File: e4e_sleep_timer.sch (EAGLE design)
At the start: 0 parts

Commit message: Added regulator, external power
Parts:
- added P1: XT60, XT60:XT60
- added U1: NUCLEO-G071RB, NUCLEO-F401RE:NUCLEO-G071RB
- added U2: 1224-5-150W, KNACRO_Regulator:1224-5-150W
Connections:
- new net +5V: U1G$1.E5V, U2.VOUT
- new net GND: P1.GND, U1G$1.GND_S1, U1G$2.AGND, U1G$2.GND_S2, U2.GND
- new net VEXT: P1.VCC, U2.VIN
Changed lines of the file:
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@@
 <parts>
 <part name="FRAME1" library="frames" library_urn="urn:adsk.eagle:library:229" deviceset="LETTER_L" device=""/>
+<part name="U1" library="NUCLEO-F401RE" deviceset="NUCLEO-G071RB" device=""/>
+<part name="SUPPLY1" library="supply2" library_urn="urn:adsk.eagle:library:372" deviceset="GND" device=""/>
+<part name="SUPPLY2" library="supply2" library_urn="urn:adsk.eagle:library:372" deviceset="GND" device=""/>
+<part name="P+1" library="supply1" library_urn="urn:adsk.eagle:library:371" deviceset="+5V" device=""/>
+<part name="FRAME2" library="frames" library_urn="urn:adsk.eagle:library:229" deviceset="LETTER_L" device=""/>
+<part name="P1" library="XT60" deviceset="XT60" device=""/>
+<part name="SUPPLY4" library="supply2" library_urn="urn:adsk.eagle:library:372" deviceset="GND" device=""/>
+<part name="U2" library="KNACRO_Regulator" deviceset="1224-5-150W" device=""/>
+<part name="SUPPLY5" library="supply2" library_urn="urn:adsk.eagle:library:372" deviceset="GND" device=""/>
+<part name="P+2" library="supply1" library_urn="urn:adsk.eagle:library:371" deviceset="+5V" device=""/>
 </parts>
 <sheets>
+<sheet>
+<plain>
+</plain>
+<instances>
+<instance part="FRAME2" gate="G$1" x="0" y="0" smashed="yes"/>
+<instance part="FRAME2" gate="G$2" x="147.32" y="0" smashed="yes">
+<attribute name="LAST_DATE_TIME" x="160.02" y="1.27" size="2.54" layer="94"/>
+<attribute name="SHEET" x="233.68" y="1.27" size="2.54" layer="94"/>
+<attribute name="DRAWING_NAME" x="165.1" y="19.05" size="2.54" layer="94"/>
+</instance>
+<instance part="P1" gate="G$1" x="25.4" y="160.02" smashed="yes" rot="R180"/>
+<instance part="SUPPLY4" gate="GND" x="30.48" y="154.94" smashed="yes">
+<attribute name="VALUE" x="28.575" y="151.765" size="1.778" layer="96"/>
+</instance>
+<instance part="U2" gate="G$1" x="106.68" y="160.02" smashed="yes">
+<attribute name="NAME" x="96.52" y="165.1" size="1.778" layer="95"/>
+<attribute name="VALUE" x="96.52" y="147.32" size="1.778" layer="96"/>
+</instance>
+<instance part="SUPPLY5" gate="GND" x="91.44" y="152.4" smashed="yes">
+<attribute name="VALUE" x="89.535" y="149.225" size="1.778" layer="96"/>
+</instance>
+<instance part="P+2" gate="1" x="129.54" y="167.64" smashed="yes">
+<attribute name="VALUE" x="127" y="162.56" size="1.778" layer="96" rot="R90"/>
+</instance>
+</instances>
+<busses>
+</busses>
+<nets>
+<net name="VEXT" class="0">
+<segment>
+<pinref part="P1" gate="G$1" pin="VCC"/>
+<wire x1="30.48" y1="162.56" x2="38.1" y2="162.56" width="0.1524" layer="91"/>
+<label x="38.1" y="162.56" size="1.778" layer="95"/>
+</segment>
+<segment>
+<pinref part="U2" gate="G$1" pin="VIN"/>
+<wire x1="91.44" y1="160.02" x2="81.28" y2="160.02" width="0.1524" layer="91"/>
+<label x="81.28" y="160.02" size="1.778" layer="95"/>
+</segment>
+</net>
+<net name="GND" class="0">
+<segment>
+<pinref part="P1" gate="G$1" pin="GND"/>
+<pinref part="SUPPLY4" gate="GND" pin="GND"/>
+</segment>
+<segment>
+<pinref part="U2" gate="G$1" pin="GND"/>
+<pinref part="SUPPLY5" gate="GND" pin="GND"/>
+</segment>
+</net>
+<net name="+5V" class="0">
+<segment>
+<pinref part="U2" gate="G$1" pin="VOUT"/>
+<wire x1="121.92" y1="160.02" x2="129.54" y2="160.02" width="0.1524" layer="91"/>
+<pinref part="P+2" gate="1" pin="+5V"/>
+<wire x1="129.54" y1="165.1" x2="129.54" y2="160.02" width="0.1524" layer="91"/>
+</segment>
+</net>
+</nets>
+</sheet>
 <sheet>
 <plain>
@@
 <attribute name="DRAWING_NAME" x="165.1" y="19.05" size="2.54" layer="94"/>
 </instance>
+<instance part="U1" gate="G$4" x="17.78" y="152.4" smashed="yes">
+<attribute name="NAME" x="12.7" y="166.37" size="1.778" layer="95"/>
+<attribute name="VALUE" x="12.7" y="138.43" size="1.778" layer="96" rot="MR180"/>
+</instance>
+<instance part="U1" gate="G$5" x="48.26" y="152.4" smashed="yes">
+<attribute name="NAME" x="43.18" y="161.29" size="1.778" layer="95"/>
+<attribute name="VALUE" x="43.18" y="140.97" size="1.778" layer="96" rot="MR180"/>
+</instance>
+<instance part="U1" gate="G$1" x="55.88" y="78.74" smashed="yes">
+<attribute name="NAME" x="40.64" y="120.65" size="1.778" layer="95"/>
+<attribute name="VALUE" x="40.64" y="34.29" size="1.778" layer="96" rot="MR180"/>
+</instance>
+<instance part="U1" gate="G$2" x="124.46" y="81.28" smashed="yes">
+<attribute name="NAME" x="111.76" y="120.65" size="1.778" layer="95"/>
+<attribute name="VALUE" x="111.76" y="39.37" size="1.778" layer="96" rot="MR180"/>
+</instance>
+<instance part="U1" gate="G$3" x="175.26" y="132.08" smashed="yes">
+<attribute name="NAME" x="165.1" y="148.59" size="1.778" layer="95"/>
+<attribute name="VALUE" x="165.1" y="113.03" size="1.778" layer="96" rot="MR180"/>
+</instance>
+<instance part="U1" gate="G$6" x="220.98" y="129.54" smashed="yes">
+<attribute name="NAME" x="210.82" y="140.97" size="1.778" layer="95"/>
+<attribute name="VALUE" x="210.82" y="115.57" size="1.778" layer="96" rot="MR180"/>
+</instance>
+<instance part="SUPPLY1" gate="GND" x="76.2" y="35.56" smashed="yes">
+<attribute name="VALUE" x="74.295" y="32.385" size="1.778" layer="96"/>
+</instance>
+<instance part="SUPPLY2" gate="GND" x="142.24" y="40.64" smashed="yes">
+<attribute name="VALUE" x="140.335" y="37.465" size="1.778" layer="96"/>
+</instance>
+<instance part="P+1" gate="1" x="81.28" y="116.84" smashed="yes">
+<attribute name="VALUE" x="78.74" y="111.76" size="1.778" layer="96" rot="R90"/>
+</instance>
 </instances>
 <busses>
 </busses>
 <nets>
+<net name="GND" class="0">
+<segment>
+<pinref part="U1" gate="G$1" pin="GND_S1"/>
+<pinref part="SUPPLY1" gate="GND" pin="GND"/>
+</segment>
+<segment>
+<pinref part="U1" gate="G$2" pin="GND_S2"/>
+<pinref part="SUPPLY2" gate="GND" pin="GND"/>
+<pinref part="U1" gate="G$2" pin="AGND"/>
+<wire x1="142.24" y1="45.72" x2="142.24" y2="43.18" width="0.1524" layer="91"/>
+<junction x="142.24" y="43.18"/>
+</segment>
+</net>
+<net name="+5V" class="0">
+<segment>
+<pinref part="P+1" gate="1" pin="+5V"/>
+<wire x1="81.28" y1="114.3" x2="81.28" y2="111.76" width="0.1524" layer="91"/>
+<pinref part="U1" gate="G$1" pin="E5V"/>
+<wire x1="81.28" y1="111.76" x2="76.2" y2="111.76" width="0.1524" layer="91"/>
+</segment>
+</net>
 </nets>
 </sheet>

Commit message: Completed PCB design
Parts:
- added P2: 10129378-906001BLF, con-lstb:MA06-1
- added P3: XT30PW-F, XT60:XT30PW-F
- added Q1: PJA3416AE_R1_00001, PJA3416AE_R1_00001:PJA3416AE_R1_00001
- added R1, R2, R5: 0, rcl:R-EU_R0603
- added R3: 100, rcl:R-US_R0603
- added R4: 10k, rcl:R-US_R0603
- added TP1, TP10, TP2, TP3, TP4, TP5, TP6, TP7, TP8, TP9: TPPAD1-13, testpad:TPPAD1-13
- added U$5: FH-320-NV, fuses:FH-320-NV
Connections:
- new net N$1: P2.4, R1.2, TP4.TP
- new net N$2: Q1.G, R3.1
- new net N$3: P2.5, R2.2
- new net N$4: R3.2, R4.1, R5.2
- new net N$5: Q1.D, U$5.G
- new net SYS_PWR: R5.1, TP6.TP, U1G$2.PD9
- new net USART1_RXD: R1.1, U1G$2.PC5
- new net USART1_TXD: R2.1, TP5.TP, U1G$2.PC4
- new net VDD1: P3.VCC, Q1.S, TP3.TP
- net +5V: now also TP2.TP, U$5.H
- net GND: now also P2.1, P3.GND, R4.2, TP10.TP, TP7.TP, TP8.TP, TP9.TP
- net VEXT: now also TP1.TP
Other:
- note added: "Control Port"
- note added: "MCU"
- moved on the sheet: U1G$1, U1G$2, U1G$3, U1G$4, U1G$5, U1G$6

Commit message: Finished PCB review
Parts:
- removed U$5: FH-320-NV, fuses:FH-320-NV
- added Q2: PJA3416AE_R1_00001, PJA3416AE_R1_00001:PJA3416AE_R1_00001
- added R6: 0, rcl:R-EU_R0603
- added TP11, TP12, TP13, TP14: TPTP20R, testpad:TPTP20R
- added U5: FH-320-NV, fuses:FH-320-NV
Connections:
- new net N$6: TP11.TP, U1G$1.VIN_S1
- new net N$7: R6.1, U1G$2.AGND
- new net N$8: TP13.TP, U1G$2.U5V
- new net N$9: TP14.TP, U1G$1.VBAT
- net +5V: now also U5.H; no longer U$5.H
- net GND: now also R6.2; no longer U1G$2.AGND
- net N$2: now also Q2.G
- net N$5: now also Q2.D, TP12.TP, U5.G; no longer U$5.G
- net VDD1: now also Q2.S
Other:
- moved on the sheet: P2, Q1, R1, R2, R3, R4, R5, TP4, TP5, TP6

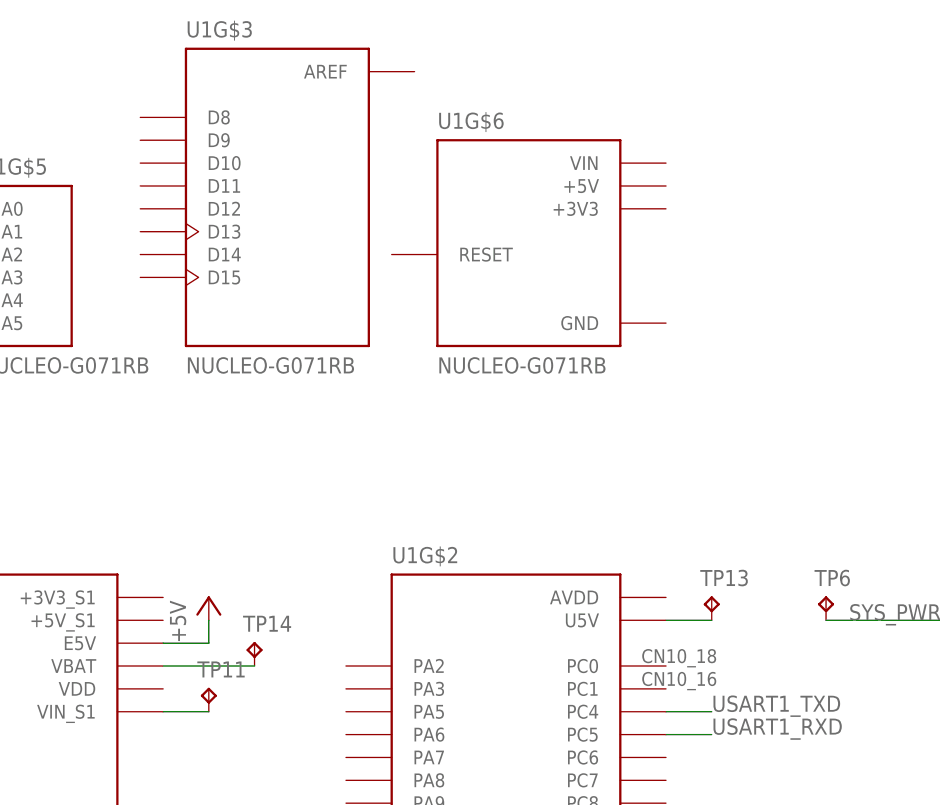
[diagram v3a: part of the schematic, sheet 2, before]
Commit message: Added Nucleo Board power bypass
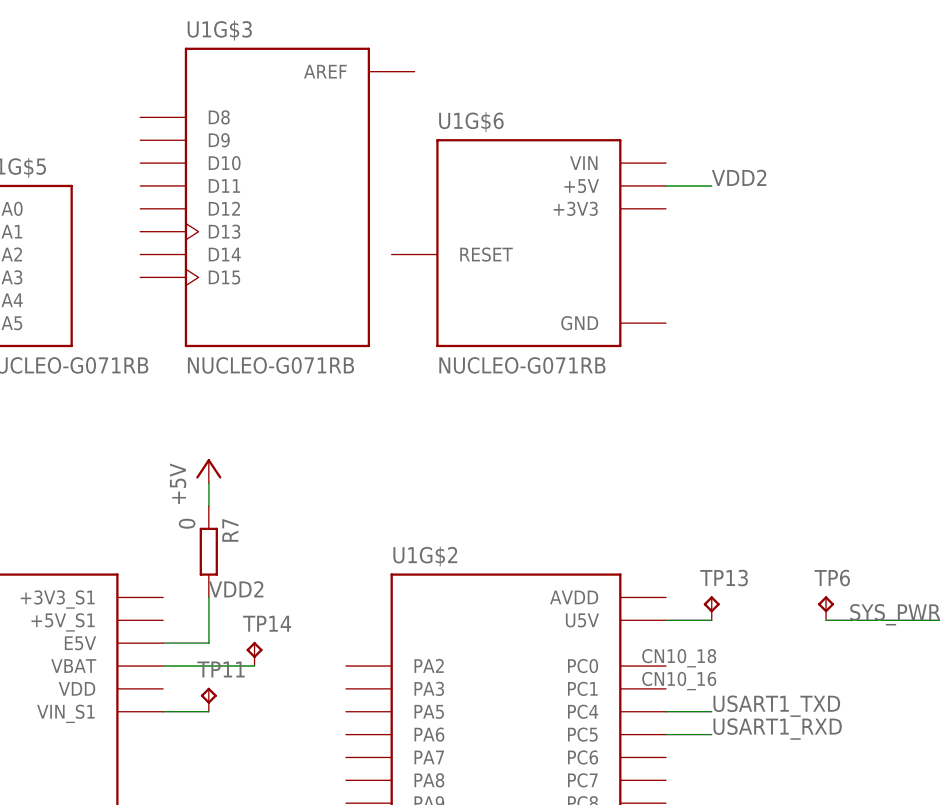
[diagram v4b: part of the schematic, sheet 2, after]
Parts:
- added R7: 0, rcl:R-EU_R0603
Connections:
- new net VDD2: R7.2, U1G$1.E5V, U1G$6.+5V
- net +5V: now also R7.1; no longer U1G$1.E5V
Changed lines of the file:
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@@
 <part name="TP13" library="testpad" library_urn="urn:adsk.eagle:library:385" deviceset="TP" device="TP20R" package3d_urn="urn:adsk.eagle:package:27973/1"/>
 <part name="TP14" library="testpad" library_urn="urn:adsk.eagle:library:385" deviceset="TP" device="TP20R" package3d_urn="urn:adsk.eagle:package:27973/1"/>
+<part name="R7" library="rcl" library_urn="urn:adsk.eagle:library:334" deviceset="R-EU_" device="R0603" package3d_urn="urn:adsk.eagle:package:23555/3" value="0"/>
 </parts>
 <sheets>
@@
 <attribute name="VALUE" x="104.775" y="27.305" size="1.778" layer="96"/>
 </instance>
-<instance part="P+1" gate="1" x="55.88" y="106.68" smashed="yes">
-<attribute name="VALUE" x="53.34" y="101.6" size="1.778" layer="96" rot="R90"/>
+<instance part="P+1" gate="1" x="55.88" y="121.92" smashed="yes">
+<attribute name="VALUE" x="53.34" y="116.84" size="1.778" layer="96" rot="R90"/>
 </instance>
 <instance part="P2" gate="1" x="238.76" y="162.56" smashed="yes" rot="R180">
@@
 <attribute name="NAME" x="59.69" y="102.87" size="1.778" layer="95"/>
 <attribute name="TP_SIGNAL_NAME" x="62.23" y="100.33" size="1.778" layer="97"/>
+</instance>
+<instance part="R7" gate="G$1" x="55.88" y="111.76" smashed="yes" rot="R270">
+<attribute name="NAME" x="57.3786" y="115.57" size="1.778" layer="95" rot="R270"/>
+<attribute name="VALUE" x="52.578" y="115.57" size="1.778" layer="96" rot="R270"/>
 </instance>
 </instances>
@@
 <net name="+5V" class="0">
 <segment>
-<pinref part="P+1" gate="1" pin="+5V"/>
-<wire x1="55.88" y1="104.14" x2="55.88" y2="101.6" width="0.1524" layer="91"/>
-<pinref part="U1" gate="G$1" pin="E5V"/>
-<wire x1="55.88" y1="101.6" x2="50.8" y2="101.6" width="0.1524" layer="91"/>
-</segment>
-<segment>
 <pinref part="P+3" gate="1" pin="+5V"/>
 <pinref part="U5" gate="A" pin="H"/>
 <wire x1="180.34" y1="142.24" x2="180.34" y2="139.7" width="0.1524" layer="91"/>
+</segment>
+<segment>
+<pinref part="R7" gate="G$1" pin="1"/>
+<pinref part="P+1" gate="1" pin="+5V"/>
+<wire x1="55.88" y1="116.84" x2="55.88" y2="119.38" width="0.1524" layer="91"/>
 </segment>
 </net>
@@
 </segment>
 </net>
+<net name="VDD2" class="0">
+<segment>
+<pinref part="U1" gate="G$1" pin="E5V"/>
+<pinref part="R7" gate="G$1" pin="2"/>
+<wire x1="50.8" y1="101.6" x2="55.88" y2="101.6" width="0.1524" layer="91"/>
+<wire x1="55.88" y1="101.6" x2="55.88" y2="106.68" width="0.1524" layer="91"/>
+<label x="55.88" y="106.68" size="1.778" layer="95"/>
+</segment>
+<segment>
+<pinref part="U1" gate="G$6" pin="+5V"/>
+<wire x1="106.68" y1="152.4" x2="111.76" y2="152.4" width="0.1524" layer="91"/>
+<label x="111.76" y="152.4" size="1.778" layer="95"/>
+</segment>
+</net>
